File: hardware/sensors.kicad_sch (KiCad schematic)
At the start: 0 parts

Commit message: changed pcb version
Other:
- removed sheet Pressure Buffer3
- sheet Pressure Buffer ports: added AIR_R, AIR_SENSOR; removed opa_output, sensor_input
- sheet Pressure Buffer1 ports: added AIR_R, AIR_SENSOR; removed opa_output, sensor_input
- sheet Pressure Buffer2 ports: added AIR_R, AIR_SENSOR; removed opa_output, sensor_input

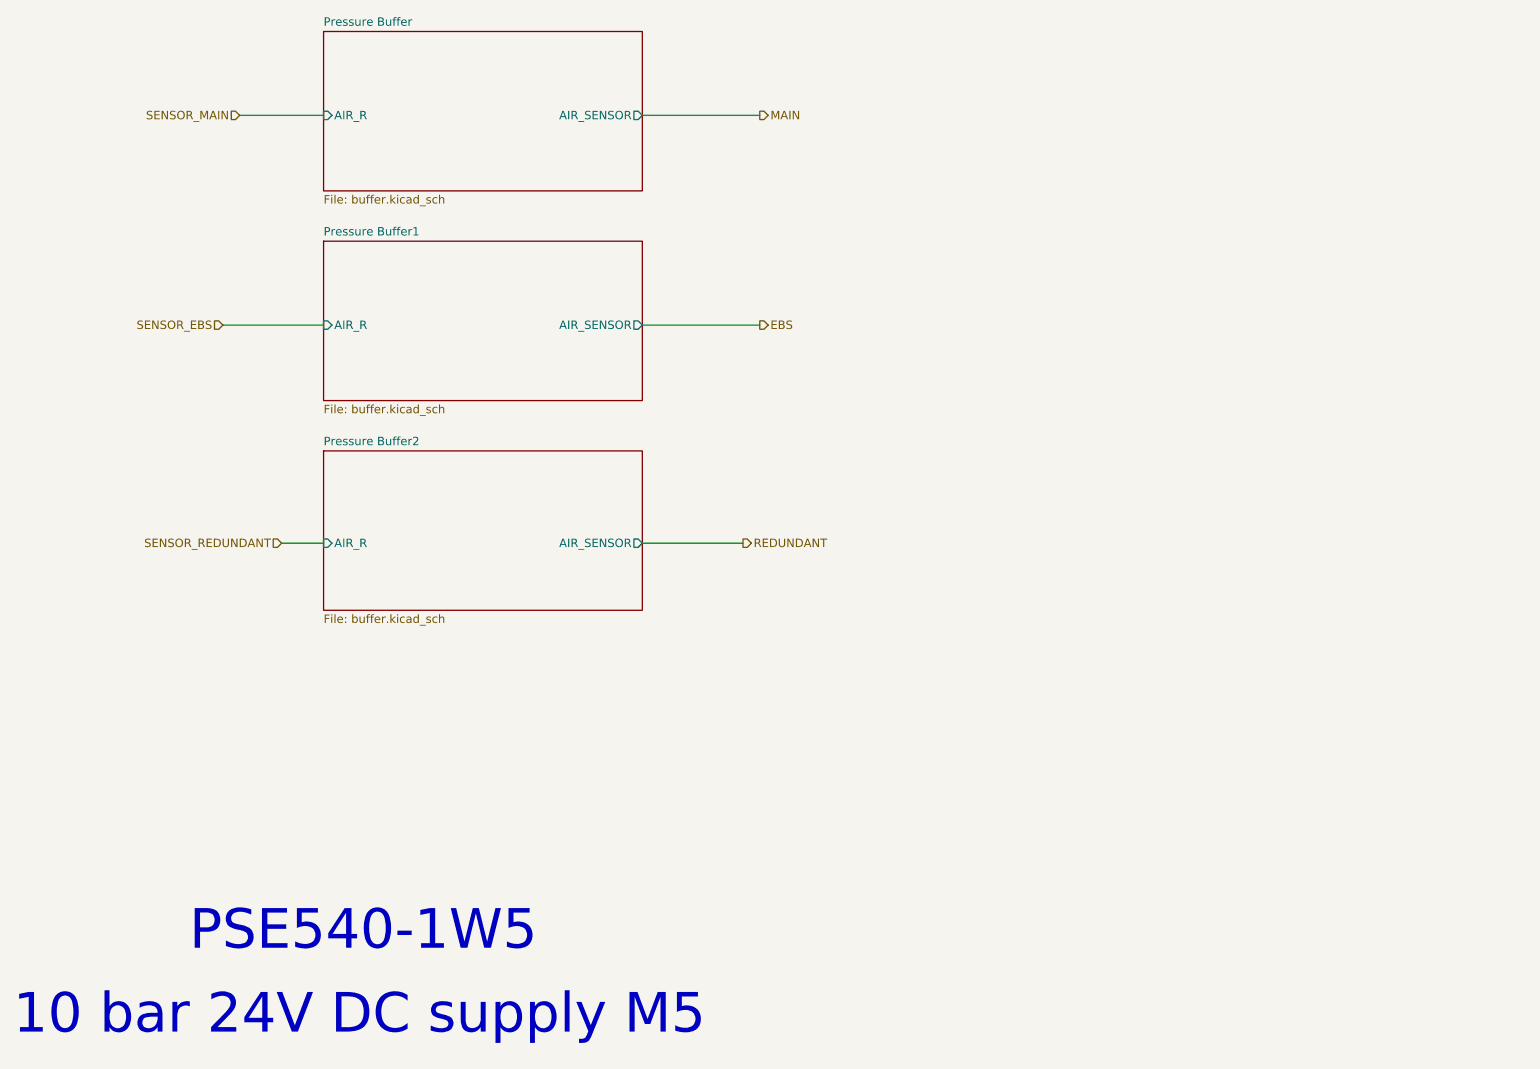
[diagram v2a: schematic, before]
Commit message: Schematic redesign for 23 rules, new pressure buffer, protection fix
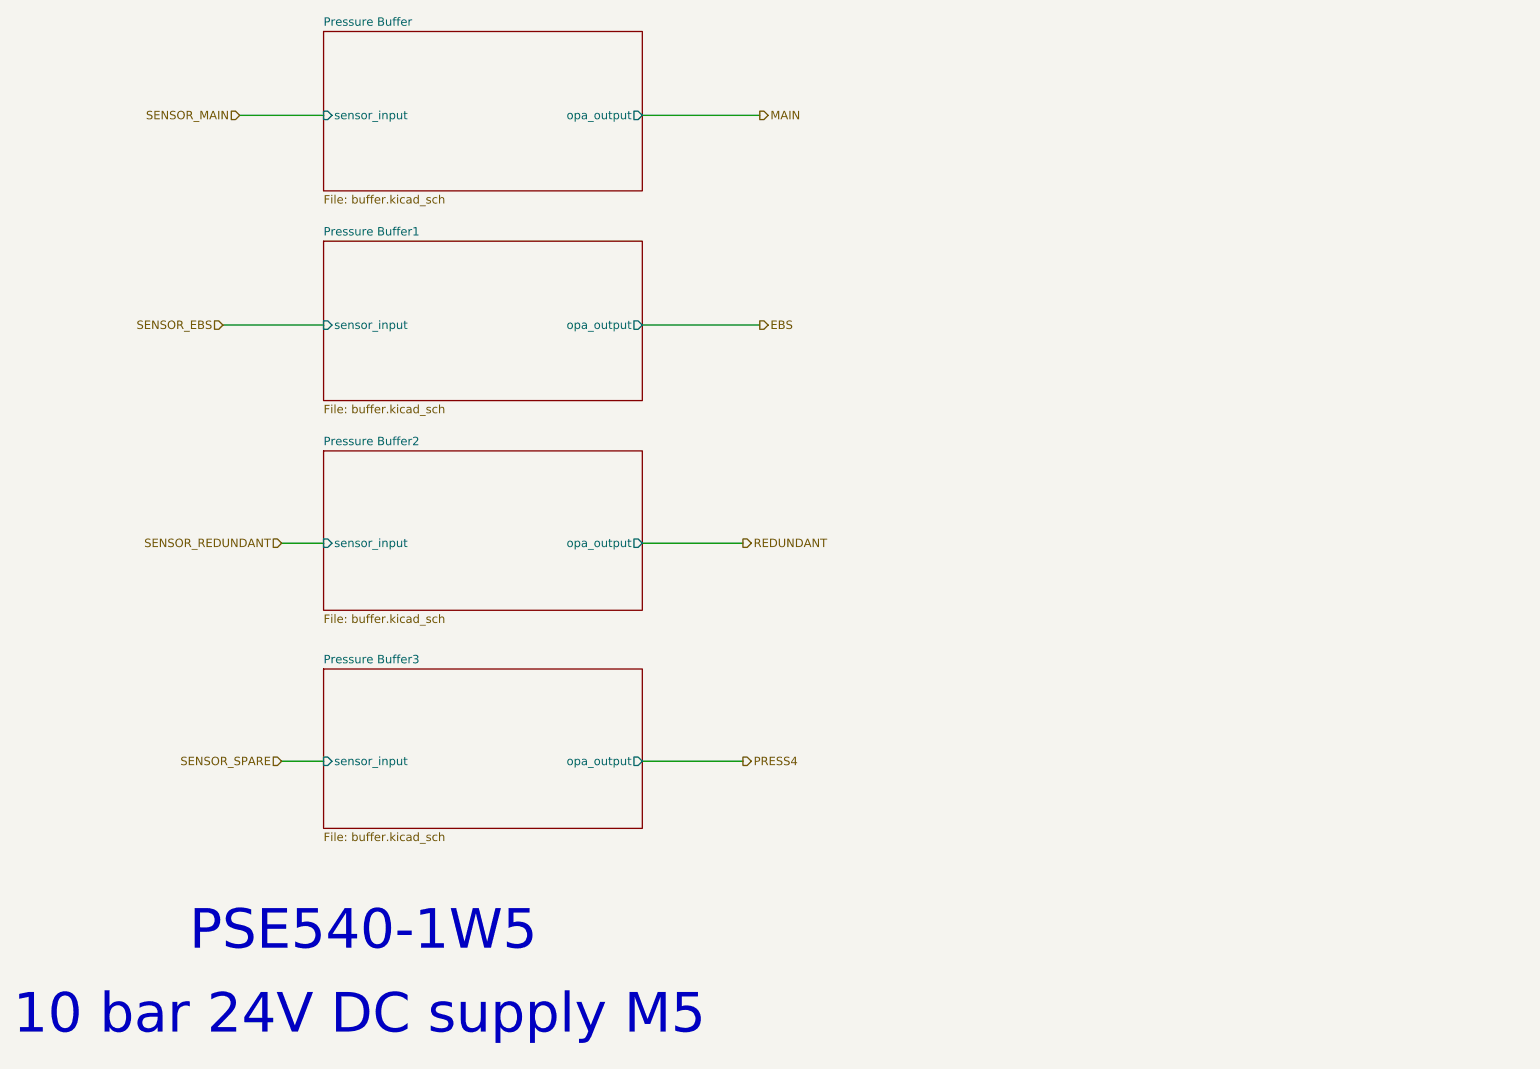
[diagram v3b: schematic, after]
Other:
- added sheet Pressure Buffer3 (buffer.kicad_sch)
- sheet Pressure Buffer ports: added opa_output, sensor_input; removed AIR_R, AIR_SENSOR
- sheet Pressure Buffer1 ports: added opa_output, sensor_input; removed AIR_R, AIR_SENSOR
- sheet Pressure Buffer2 ports: added opa_output, sensor_input; removed AIR_R, AIR_SENSOR
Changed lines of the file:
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@@
+    (stroke (width 0) (type default))
+  )
+  (wire (pts (xy 93.98 149.86) (xy 100.33 149.86))
     (stroke (width 0) (type default))
   )
@@
     (stroke (width 0) (type default))
   )
+  (wire (pts (xy 148.59 149.86) (xy 163.83 149.86))
+    (stroke (width 0) (type default))
+  )
   (text "10 bar 24V DC supply M5" (at 53.34 191.77 0)
     (effects (font (size 6 6)) (justify left bottom))
@@
   (text "PSE540-1W5" (at 80.01 179.07 0)
     (effects (font (size 6 6)) (justify left bottom))
+  )
+  (hierarchical_label "PRESS4" (shape output) (at 163.83 149.86 0) (fields_autoplaced)
+    (effects (font (size 1.27 1.27)) (justify left))
   )
   (hierarchical_label "REDUNDANT" (shape output) (at 163.83 116.84 0) (fields_autoplaced)
@@
     (effects (font (size 1.27 1.27)) (justify left))
   )
+  (hierarchical_label "SENSOR_SPARE" (shape input) (at 93.98 149.86 180) (fields_autoplaced)
+    (effects (font (size 1.27 1.27)) (justify right))
+  )
   (hierarchical_label "SENSOR_EBS" (shape input) (at 85.09 83.82 180) (fields_autoplaced)
     (effects (font (size 1.27 1.27)) (justify right))
@@
       (effects (font (size 1.27 1.27)) (justify left top))
     )
-    (pin "AIR_SENSOR" output (at 148.59 83.82 0)
+    (pin "sensor_input" input (at 100.33 83.82 180)
+      (effects (font (size 1.27 1.27)) (justify left))
+    )
+    (pin "opa_output" output (at 148.59 83.82 0)
       (effects (font (size 1.27 1.27)) (justify right))
-    )
-    (pin "AIR_R" input (at 100.33 83.82 180)
-      (effects (font (size 1.27 1.27)) (justify left))
     )
     (instances
@@
       (effects (font (size 1.27 1.27)) (justify left top))
     )
-    (pin "AIR_SENSOR" output (at 148.59 52.07 0)
+    (pin "sensor_input" input (at 100.33 52.07 180)
+      (effects (font (size 1.27 1.27)) (justify left))
+    )
+    (pin "opa_output" output (at 148.59 52.07 0)
       (effects (font (size 1.27 1.27)) (justify right))
-    )
-    (pin "AIR_R" input (at 100.33 52.07 180)
-      (effects (font (size 1.27 1.27)) (justify left))
     )
     (instances
@@
       (effects (font (size 1.27 1.27)) (justify left top))
     )
-    (pin "AIR_SENSOR" output (at 148.59 116.84 0)
+    (pin "sensor_input" input (at 100.33 116.84 180)
+      (effects (font (size 1.27 1.27)) (justify left))
+    )
+    (pin "opa_output" output (at 148.59 116.84 0)
       (effects (font (size 1.27 1.27)) (justify right))
-    )
-    (pin "AIR_R" input (at 100.33 116.84 180)
-      (effects (font (size 1.27 1.27)) (justify left))
     )
     (instances
@@
       )
     )
+  )
+  (sheet (at 100.33 135.89) (size 48.26 24.13) (fields_autoplaced)
+    (stroke (width 0.1524) (type solid))
+    (fill (color 0 0 0 0.0000))
+    (property "Sheetname" "Pressure Buffer3" (at 100.33 135.1784 0)
+      (effects (font (size 1.27 1.27)) (justify left bottom))
+    )
+    (property "Sheetfile" "buffer.kicad_sch" (at 100.33 160.6046 0)
+      (effects (font (size 1.27 1.27)) (justify left top))
+    )
+    (pin "sensor_input" input (at 100.33 149.86 180)
+      (effects (font (size 1.27 1.27)) (justify left))
+    )
+    (pin "opa_output" output (at 148.59 149.86 0)
+      (effects (font (size 1.27 1.27)) (justify right))
+    )
+    (instances
+      (project "PUTM_DV_EBS_2023"
+        (path "/d921fbb5-521e-405d-bdec-f40195adfa1c/0e6e746e-cf7c-47e8-8ed6-c681697efa7a" (page "16"))
+      )
+    )
